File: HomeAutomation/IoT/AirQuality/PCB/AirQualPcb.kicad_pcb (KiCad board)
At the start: 2 copper layers, 55.9 x 61 mm, 12 parts, among them J1 QWIIC_CONNECTORJS-1MM, J2 QWIIC_CONNECTORJS-1MM, J3 Power Switch, Q1 ZXMN2B14FHCT, U1 Particle_Argon

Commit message: PCB laid-out.  About to start tracks.
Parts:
- removed the G*** at (181.1, 95.2)
- removed the G*** at (181.1, 86.4)
- removed the REF** at (186.7, 108.0)
- removed the REF** at (138.4, 108.0)
- removed the REF** at (138.4, 54.6)
- removed the REF** at (186.7, 54.6)
- added C1: 10uF, Capacitors:0603, F.Cu at (135.9, 61.0)
- added C2: 10uF, Capacitors:0603, F.Cu at (135.9, 72.4)
- added C3: 10uF, Capacitors:0603, F.Cu at (135.9, 74.3)
- added C4: 100nF, Capacitors:0603, F.Cu at (170.2, 101.6)
- added C5: 10uF, Capacitors:0603, F.Cu at (171.2, 68.7)
- added C6: 1uF, Capacitors:0603, F.Cu at (175.8, 68.7)
- added C7: 100nF, Capacitors:0603, F.Cu at (170.2, 74.9)
- added C8: 100nF, Capacitors:0603, F.Cu at (170.2, 83.8)
- added C9: 100nF, Capacitors:0603, F.Cu at (170.2, 92.7)
- added G***: LOGO, JohnZPCB:Qwiic_Logo, F.Cu at (181.1, 74.9)
- added G***: LOGO, JohnZPCB:Qwiic_Logo, F.Cu at (181.1, 92.7)
- added G***: LOGO, JohnZPCB:Qwiic_Logo, F.Cu at (181.1, 83.8)
- added J2: QWIIC_CONNECTORJS-1MM, Connector_JST:JST_SH_SM04B-SRSS-TB_1x04-1MP_P1.00mm_Horizontal, F.Cu at (176.5, 74.9)
- added J5: UART_CONNECTORJS-1MM, Connectors:1X04_1MM_RA, F.Cu at (174.5, 101.1)
- added L1: VLS3012HBX-2R2M‎, JohnZPCB:VLS3012HBX, F.Cu at (135.8, 64.6)
- added Q2: BSS138, digikey-footprints:SOT-23-3, F.Cu at (133.3, 91.4)
- added Q3: BSS138, digikey-footprints:SOT-23-3, F.Cu at (133.3, 97.8)
- added R2: 10K, Capacitors:0603, F.Cu at (139.2, 90.2)
- added R3: 10K, Capacitors:0603, F.Cu at (139.2, 94.0)
- added R4: 10K, Capacitors:0603, F.Cu at (139.3, 97.8)
- added R5: 10K, Capacitors:0603, F.Cu at (139.3, 101.6)
- added REF**: MountingHole_3.2mm_M3, MountingHole:MountingHole_3.2mm_M3, F.Cu at (182.9, 108.0)
- added REF**: MountingHole_3.2mm_M3, MountingHole:MountingHole_3.2mm_M3, F.Cu at (133.3, 108.0)
- added REF**: MountingHole_3.2mm_M3, MountingHole:MountingHole_3.2mm_M3, F.Cu at (133.3, 54.6)
- added REF**: MountingHole_3.2mm_M3, MountingHole:MountingHole_3.2mm_M3, F.Cu at (182.9, 54.6)
- added U1: RP402Nxx1x, Package_TO_SOT_SMD:SOT-23-5, F.Cu at (135.8, 69.0)
- J1: renamed from J3; footprint Connectors:1X02 -> Connectors:1X03
- Q1: value ZXMN2B14FHCT -> BSS138
- R1: footprint Capacitors:0603 -> Resistor_SMD:R_0603_1608Metric
- moved Q1 15.7 mm to (172.0, 61.7), turned to 270 degrees
- moved R1 11.0 mm to (177.0, 62.0), turned to 90 degrees
- moved J1 9.34 mm to (181.4, 60.2), turned to 270 degrees
- moved J3 2.54 mm to (176.5, 92.7)
- moved J4 2.54 mm to (176.5, 83.8)
- renumbered J1 to J3, J2 to J4, U1 to U2
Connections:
- Q1 pad 3: Net-(Q1-Pad3) -> Net-(J1-Pad3)
- U2 pad 27: Net-(Q1-Pad3) -> Net-(J1-Pad3)
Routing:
- net Net-(J2-Pad3): track 26.9 -> 1.34 mm
- net Net-(J2-Pad4): track 22.8 -> 0.00 mm
- net GND: track 6.53 -> 0.00 mm, vias 2 -> 0
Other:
- board size 55.9 x 61 mm -> 57.2 x 61 mm
- board text added: "5V"
- board text added: "GND"
- board text added: "John Zehetner Dec 29, 2020 Rev A"
- board text added: "NC"
- board text added: "NO"
- board text added: "Particle Argon"
- board text added: "Rx"
- board text added: "Tx"
- board text added: "Tx and Rx are swapped"

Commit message: Board mostly done
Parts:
- moved C8 4.02 mm to (171.4, 87.6), turned to 90 degrees
- moved C7 4.02 mm to (171.4, 78.7), turned to 90 degrees
- moved C9 2.62 mm to (171.4, 95.0), turned to 90 degrees
- moved C4 1.83 mm to (171.2, 103.1)
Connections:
- J3 pad MP: (no net) -> 3V3
- J5 pad NC1: (no net) -> 3V3
- J5 pad NC2: (no net) -> 3V3
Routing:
- net +5V: track 0.00 -> 98.9 mm, vias 0 -> 6
- net Net-(C1-Pad1): track 0.00 -> 59.5 mm
- net Net-(J2-Pad3): track 1.34 -> 50.7 mm
- net Net-(J5-Pad4): track 0.00 -> 49.0 mm
- net Net-(J5-Pad3): track 0.00 -> 45.8 mm
- net GND: track 0.00 -> 41.2 mm, vias 0 -> 13
- net Net-(J2-Pad4): track 0.00 -> 38.4 mm
- net Net-(J1-Pad3): track 0.00 -> 20.5 mm
- net 3V3: track 0.16 -> 13.9 mm, vias 0 -> 6
- net Net-(Q3-Pad2): track 0.00 -> 12.4 mm
- net Net-(Q2-Pad2): track 0.00 -> 12.1 mm
- net Net-(J1-Pad1): track 0.00 -> 9.07 mm
- net Net-(L1-Pad2): track 0.00 -> 6.95 mm

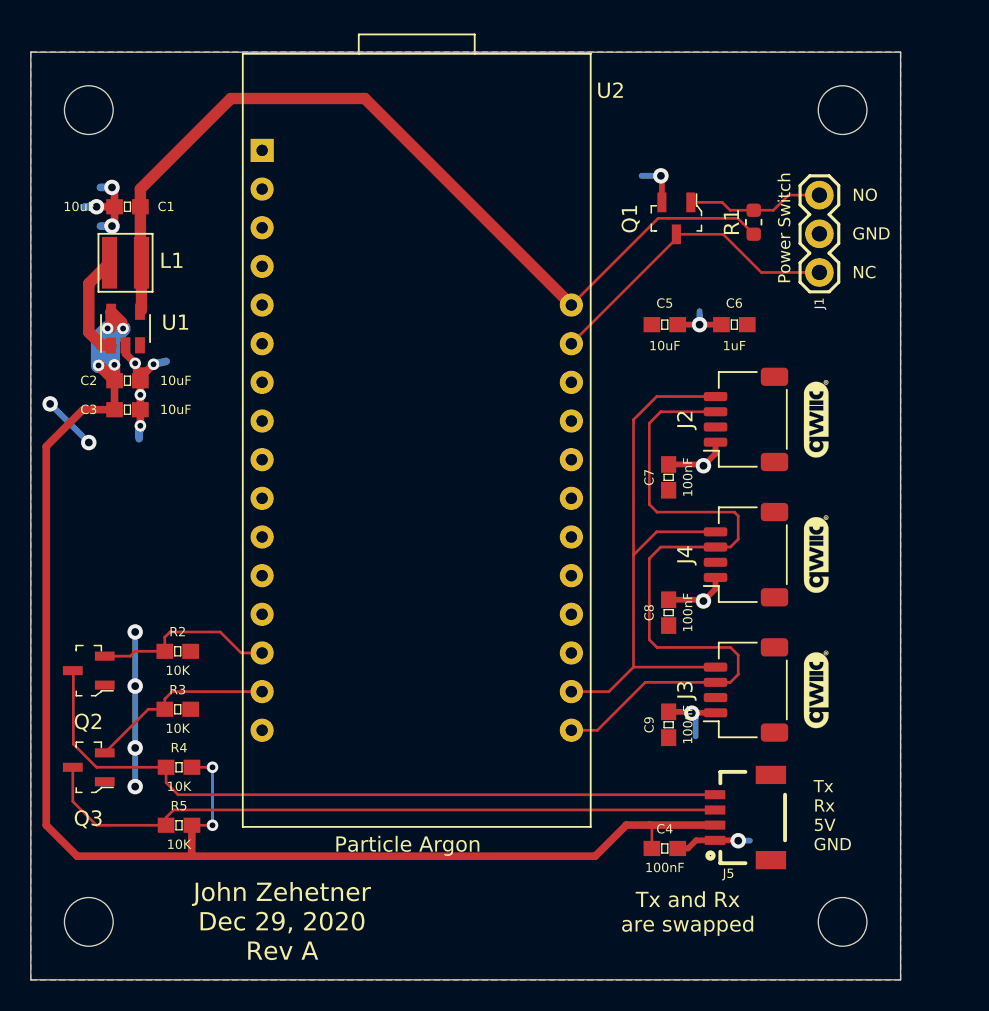
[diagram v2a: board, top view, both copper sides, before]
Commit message: About to start cutting holes in enclosure
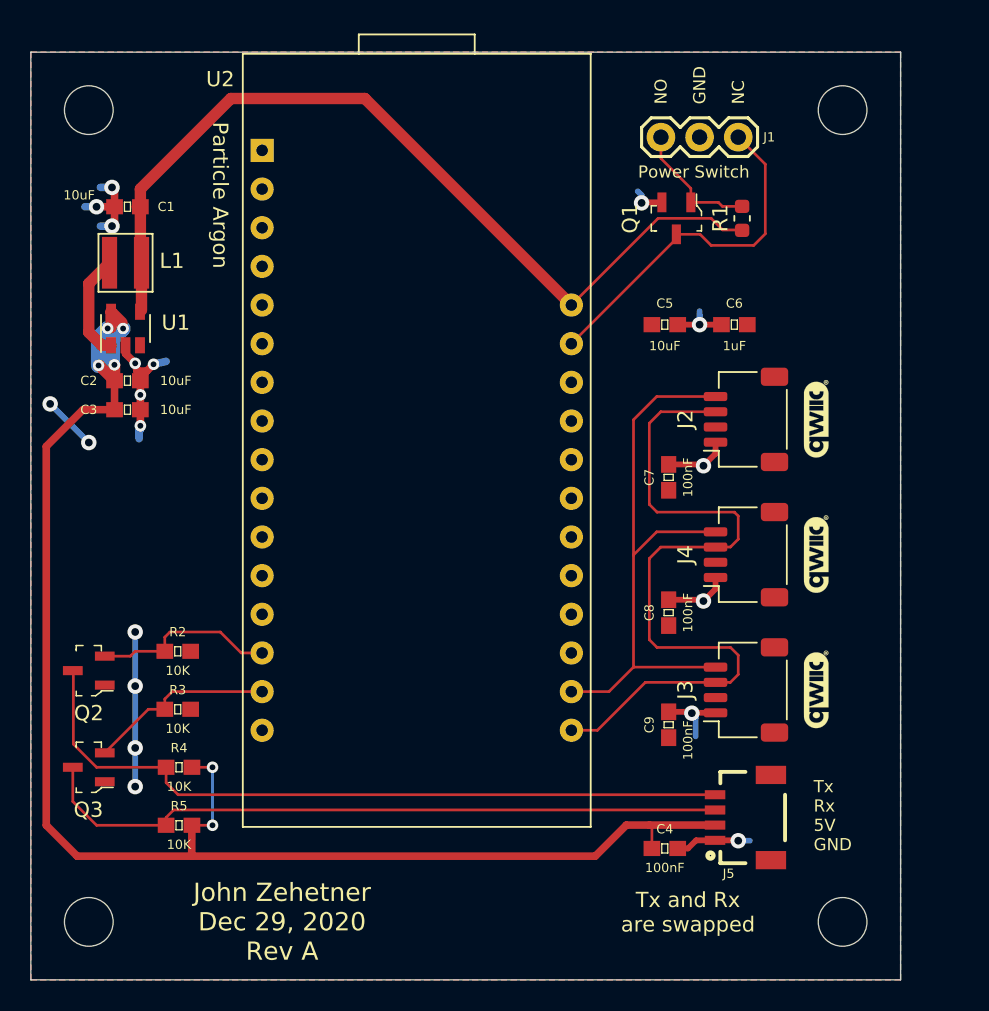
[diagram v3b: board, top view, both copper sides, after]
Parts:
- moved J1 11.1 mm to (170.9, 56.4), turned to 0 degrees
- moved R1 0.80 mm to (176.3, 61.7)
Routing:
- net Net-(J1-Pad3): track 20.5 -> 23.6 mm
- net Net-(C1-Pad1): track 59.5 -> 58.7 mm
- net GND: track 41.2 -> 40.4 mm

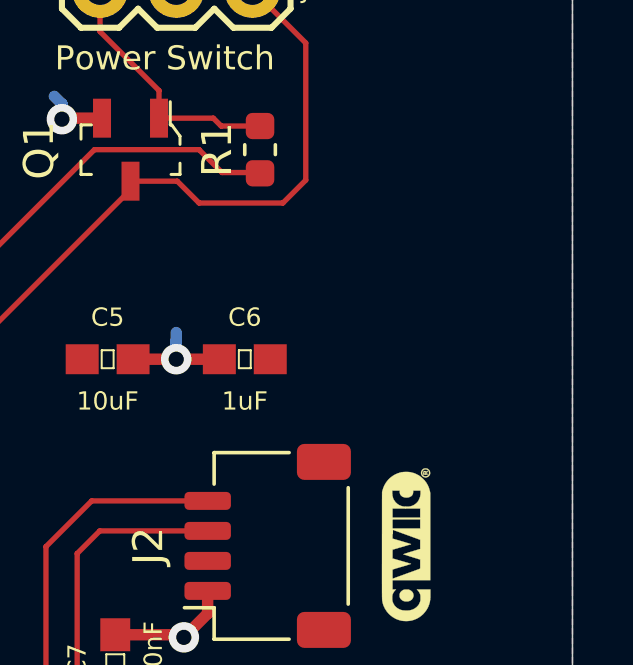
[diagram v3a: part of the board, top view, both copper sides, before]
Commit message: Add a fan power connector
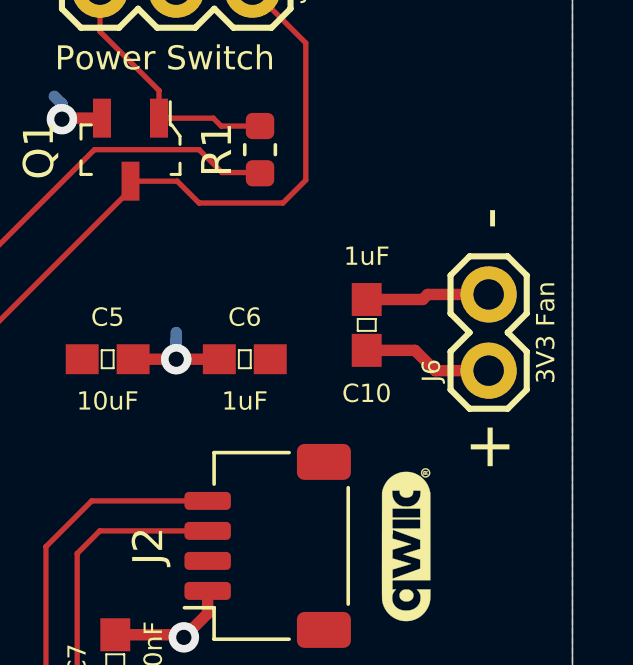
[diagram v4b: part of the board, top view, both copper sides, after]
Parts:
- added C10: 1uF, Capacitors:0603, F.Cu at (179.8, 67.6)
- added J6: 3V3 Fan, Connectors:1X02, F.Cu at (183.9, 69.1)
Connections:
- J3 pad MP: 3V3 -> (no net)
- J5 pad NC1: 3V3 -> (no net)
- J5 pad NC2: 3V3 -> (no net)
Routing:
- net 3V3: track 13.9 -> 18.3 mm
- net GND: track 40.4 -> 44.5 mm
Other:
- board text added: "+"
- board text added: "-"

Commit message: a couple last minute changes before sending to fab
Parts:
- added J1: Test Points, Connectors:1X03, F.Cu at (131.1, 81.0)
- added J6: Test Points, Connectors:1X01, F.Cu at (140.2, 56.4)
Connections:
- J3 pad MP: (no net) -> 3V3
- J5 pad NC1: (no net) -> 3V3
- J5 pad NC2: (no net) -> 3V3
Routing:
- net +5V: track 98.9 -> 99.4 mm
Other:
- board text added: "3V3"
- board text added: "B+"

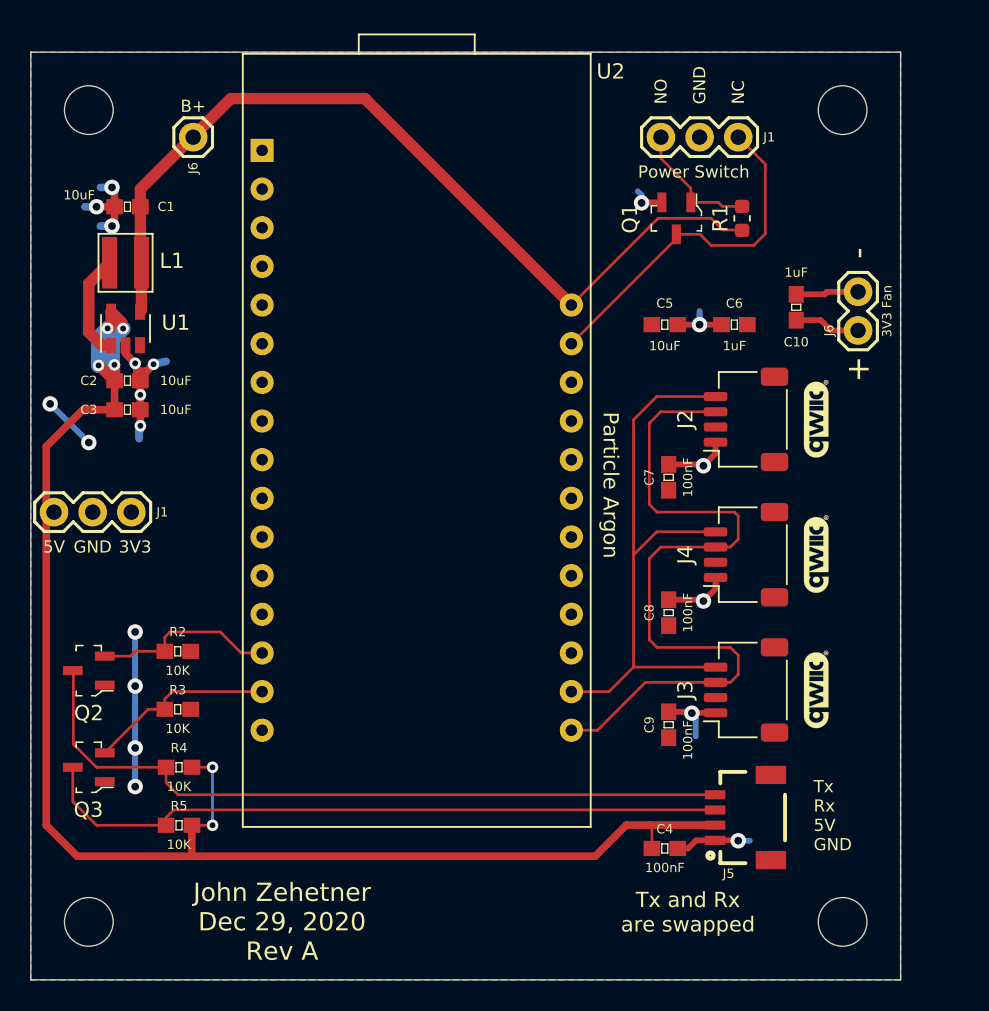
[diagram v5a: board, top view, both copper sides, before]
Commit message: PCB: change Argon footprint, direct-connect Sensirion, add button connectors
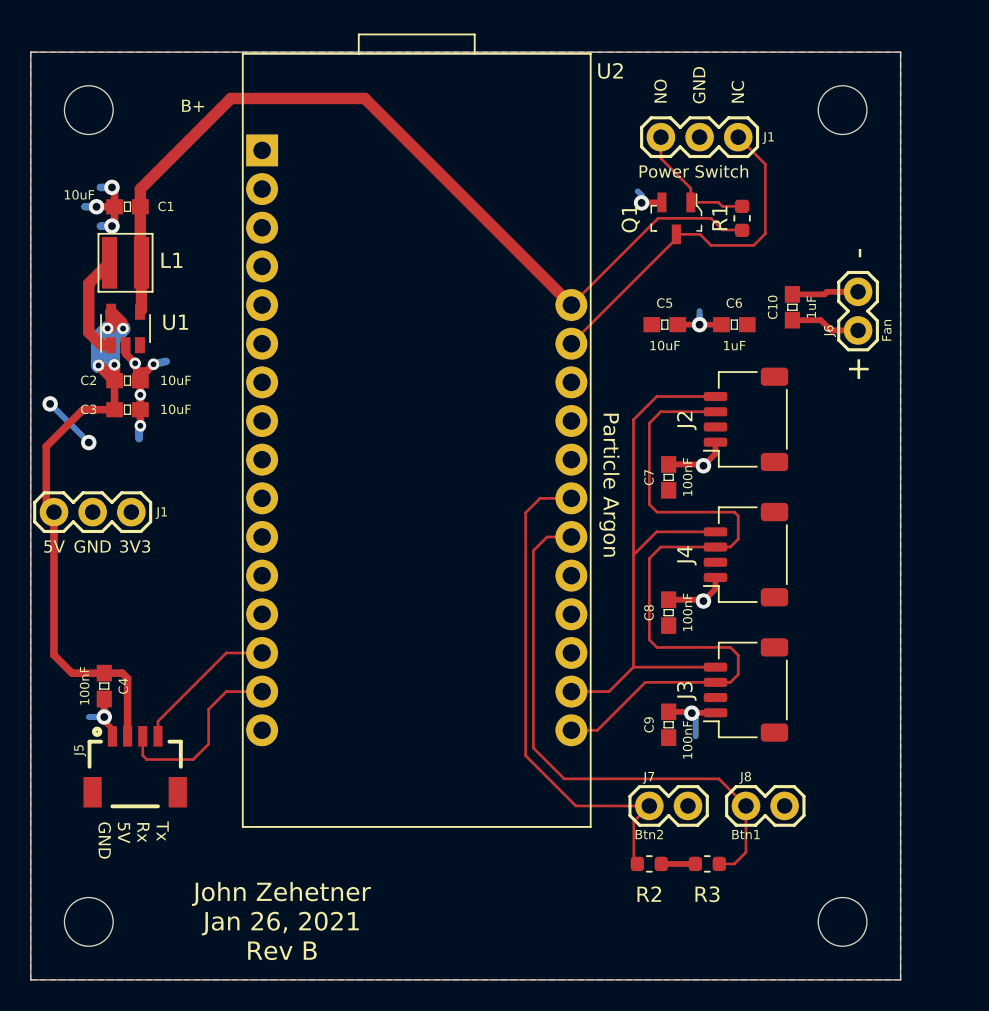
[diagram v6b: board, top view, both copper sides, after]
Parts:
- removed G*** (x3): LOGO, JohnZPCB:Qwiic_Logo
- removed the J6 at (140.2, 56.4)
- removed Q2, Q3: BSS138, digikey-footprints:SOT-23-3
- removed R4, R5: 10K, Capacitors:0603
- removed REF** (x4): MountingHole_3.2mm_M3, MountingHole:MountingHole_3.2mm_M3
- added H1: MountingHole, MountingHole:MountingHole_3.2mm_M3, F.Cu at (133.3, 54.6)
- added H2: MountingHole, MountingHole:MountingHole_3.2mm_M3, F.Cu at (182.9, 54.6)
- added H3: MountingHole, MountingHole:MountingHole_3.2mm_M3, F.Cu at (133.3, 108.0)
- added H4: MountingHole, MountingHole:MountingHole_3.2mm_M3, F.Cu at (182.9, 108.0)
- added J7: Btn2, Connectors:1X02, F.Cu at (170.2, 100.3)
- added J8: Btn1, Connectors:1X02, F.Cu at (176.5, 100.3)
- J1: value Test Points -> Power Switch
- J6: value 3V3 Fan -> Fan
- R2, R3: footprint Capacitors:0603 -> Resistor_SMD:R_0603_1608Metric
- moved J5 38.5 mm to (136.4, 95.8), turned to 0 degrees
- moved C4 38.3 mm to (134.4, 92.5), turned to 270 degrees
- moved R3 36.3 mm to (174.0, 104.1)
- moved R2 34.0 mm to (170.2, 104.1)
- moved C10 0.25 mm to (179.6, 67.6)
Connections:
- J3 pad MP: 3V3 -> (no net)
- J5 pad NC1: 3V3 -> (no net)
- J5 pad NC2: 3V3 -> (no net)
- R2 pad 1: Net-(Q2-Pad2) -> Net-(J7-Pad1)
- R3 pad 1: Net-(Q3-Pad2) -> 3V3
- R3 pad 2: 3V3 -> Net-(J8-Pad1)
- U2 pad 14: Net-(Q2-Pad2) -> Net-(J5-Pad4)
- U2 pad 15: Net-(Q3-Pad2) -> Net-(J5-Pad3)
- U2 pad 22: Net-(U2-Pad22) -> Net-(J8-Pad1)
- U2 pad 23: Net-(U2-Pad23) -> Net-(J7-Pad1)
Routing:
- net +5V: track 99.4 -> 41.8 mm, vias 6 -> 4
- net Net-(J5-Pad4): track 49.0 -> 9.69 mm
- net Net-(J8-Pad1): track 0.00 -> 36.5 mm
- net Net-(J5-Pad3): track 45.8 -> 12.4 mm
- net Net-(J7-Pad1): track 0.00 -> 33.2 mm
- net Net-(Q3-Pad2): track 12.4 -> 0.00 mm
- net Net-(Q2-Pad2): track 12.1 -> 0.00 mm
- net 3V3: track 18.3 -> 10.3 mm, vias 6 -> 2
- net GND: track 44.5 -> 43.3 mm
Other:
- board text added: "John Zehetner Jan 26, 2021 Rev B"
- board text removed: "John Zehetner Dec 29, 2020 Rev A"
- board text removed: "Tx and Rx are swapped"

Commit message: Fix power supply enable line
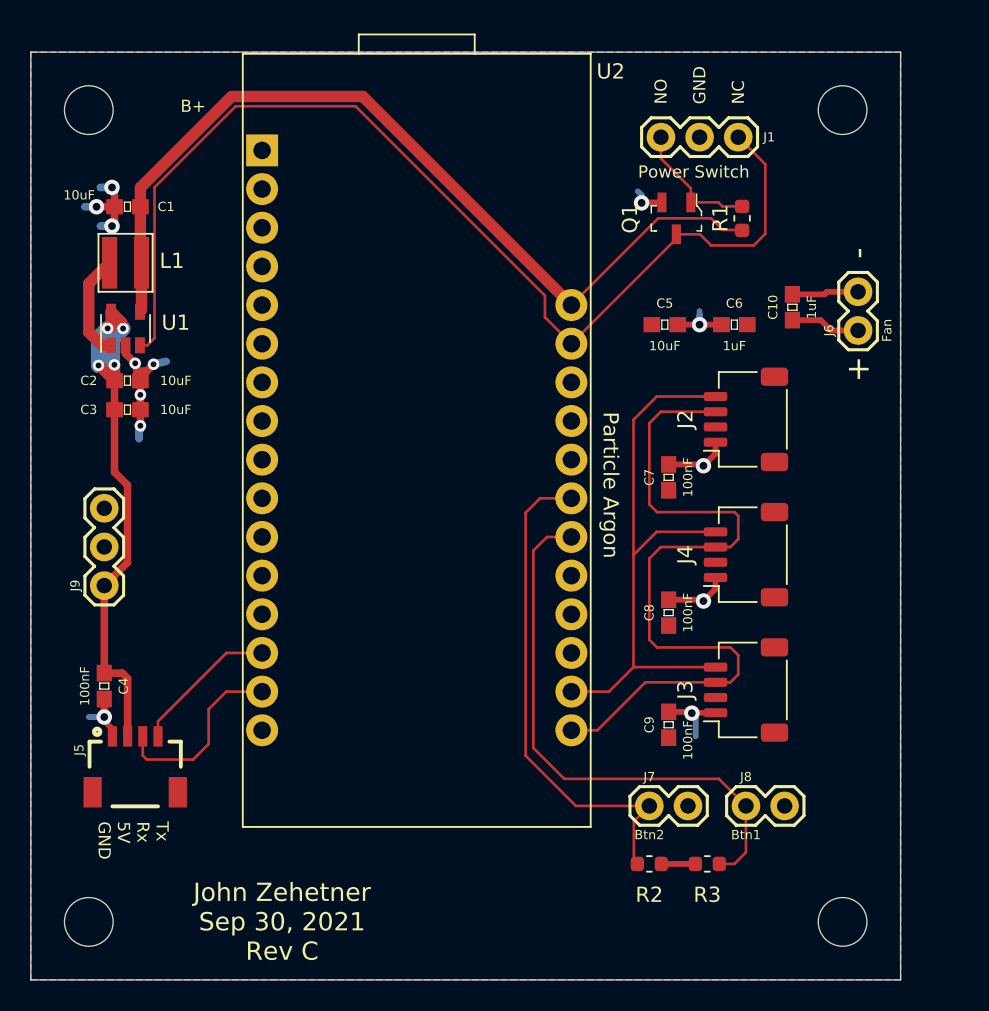
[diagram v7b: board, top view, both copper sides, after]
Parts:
- removed the J1 at (131.1, 81.0)
- added J9: Power Supply Rails, Connectors:1X03, F.Cu at (134.4, 85.9)
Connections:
- U1 pad 3: 3V3 -> Net-(J1-Pad3)
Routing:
- net Net-(J1-Pad3): track 23.6 -> 71.5 mm
- net +5V: track 41.8 -> 36.5 mm
- net 3V3: track 10.3 -> 6.74 mm, vias 2 -> 0
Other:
- board text added: "John Zehetner Sep 30, 2021 Rev C"
- board text removed: "3V3"
- board text removed: "John Zehetner Jan 26, 2021 Rev B"
